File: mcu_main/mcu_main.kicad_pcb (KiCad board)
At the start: 2 copper layers, 108 x 61.7 mm, 48 parts, among them J1 Micro_SD_Card_Det_Hirose_DM3AT, J10 Conn_01x02_Pin, J2 Conn_01x10_Pin, J3 Conn_01x06_Pin, J4 4P4C_Shielded, J5 4P4C_Shielded, J6 Screw_Terminal_01x03_ebrake, J7 Screw_Terminal_01x03_throttle, J8 Screw_Terminal_01x06, J9 Conn_01x14_Socket, U1 ESP32-S3-WROOM-1, U2 USB_C_connector, U3 SGM2212-3.3, U4 VL53L1CXV0FY1, sw1 SW_Push_Dual, sw2 SW_Push_Dual

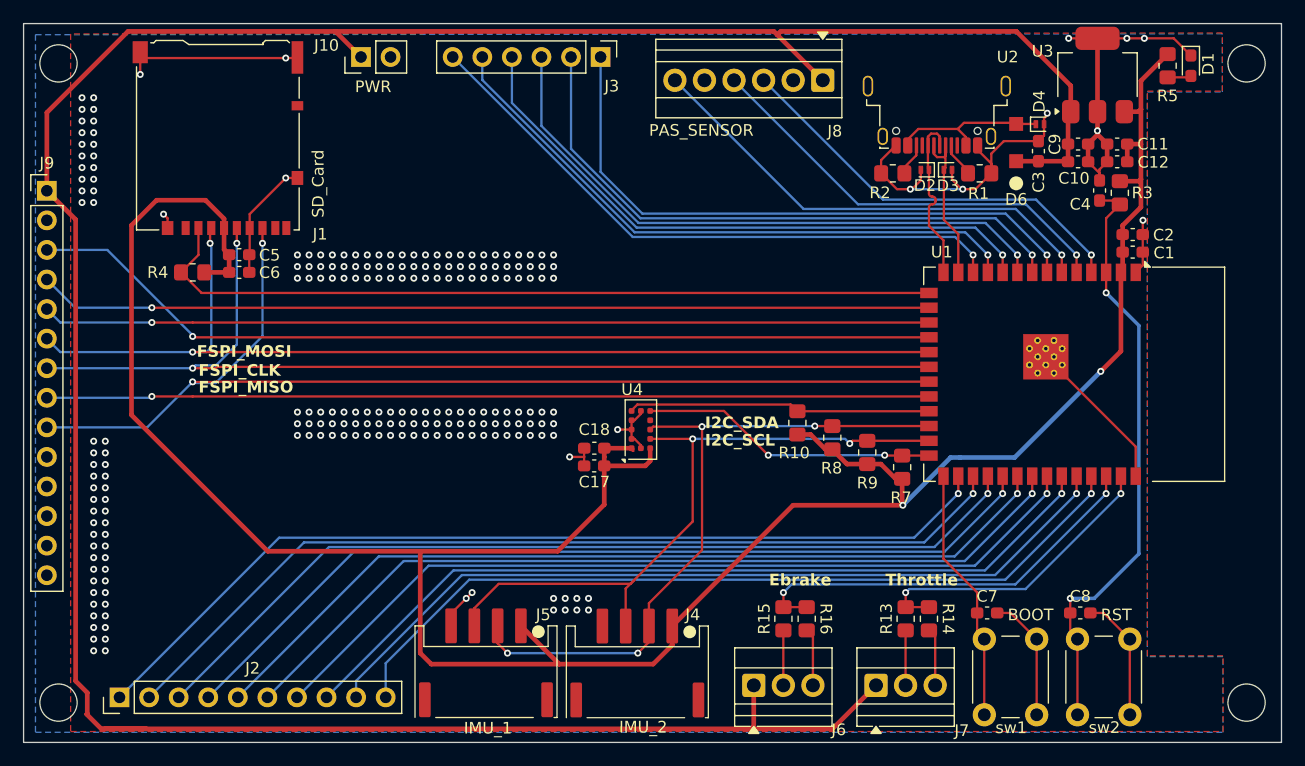
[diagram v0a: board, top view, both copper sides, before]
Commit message: stitching vias
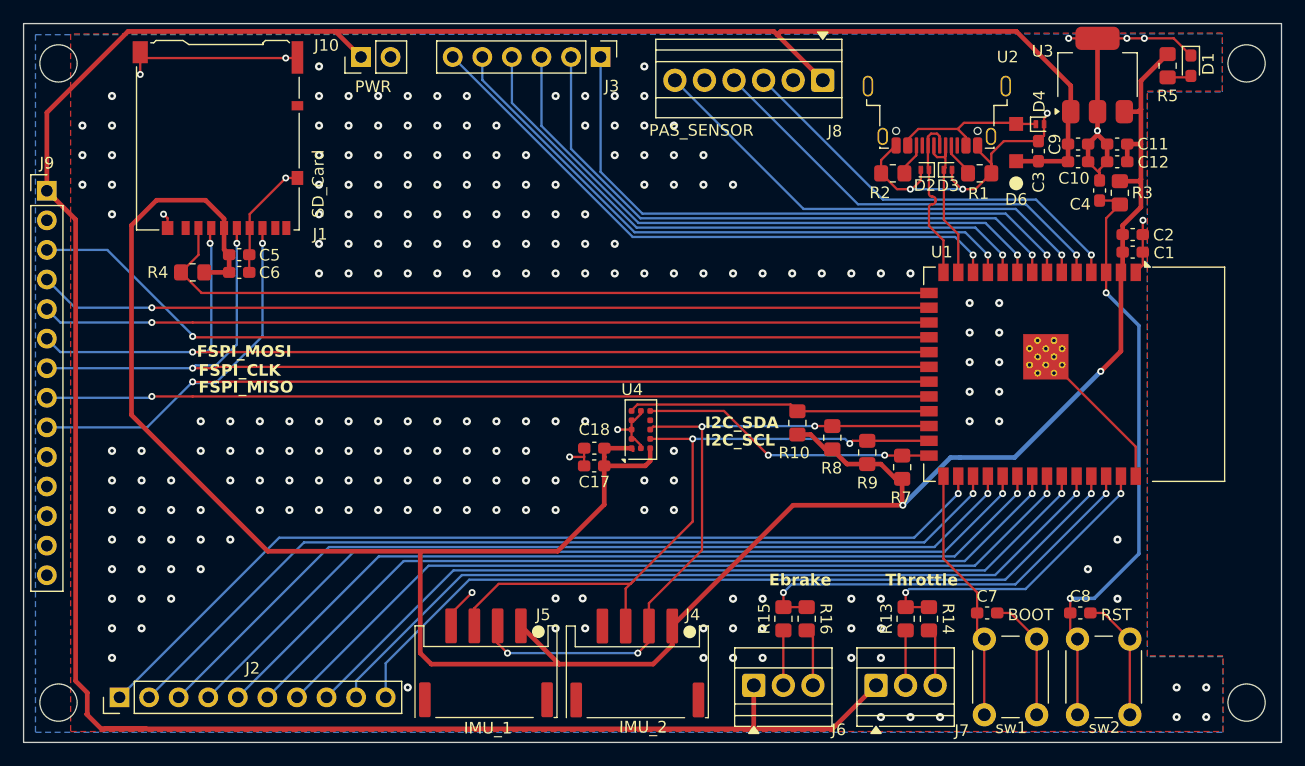
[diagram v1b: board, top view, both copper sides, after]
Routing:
- net GND: vias 220 -> 230

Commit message: test points and silkscreen annotations
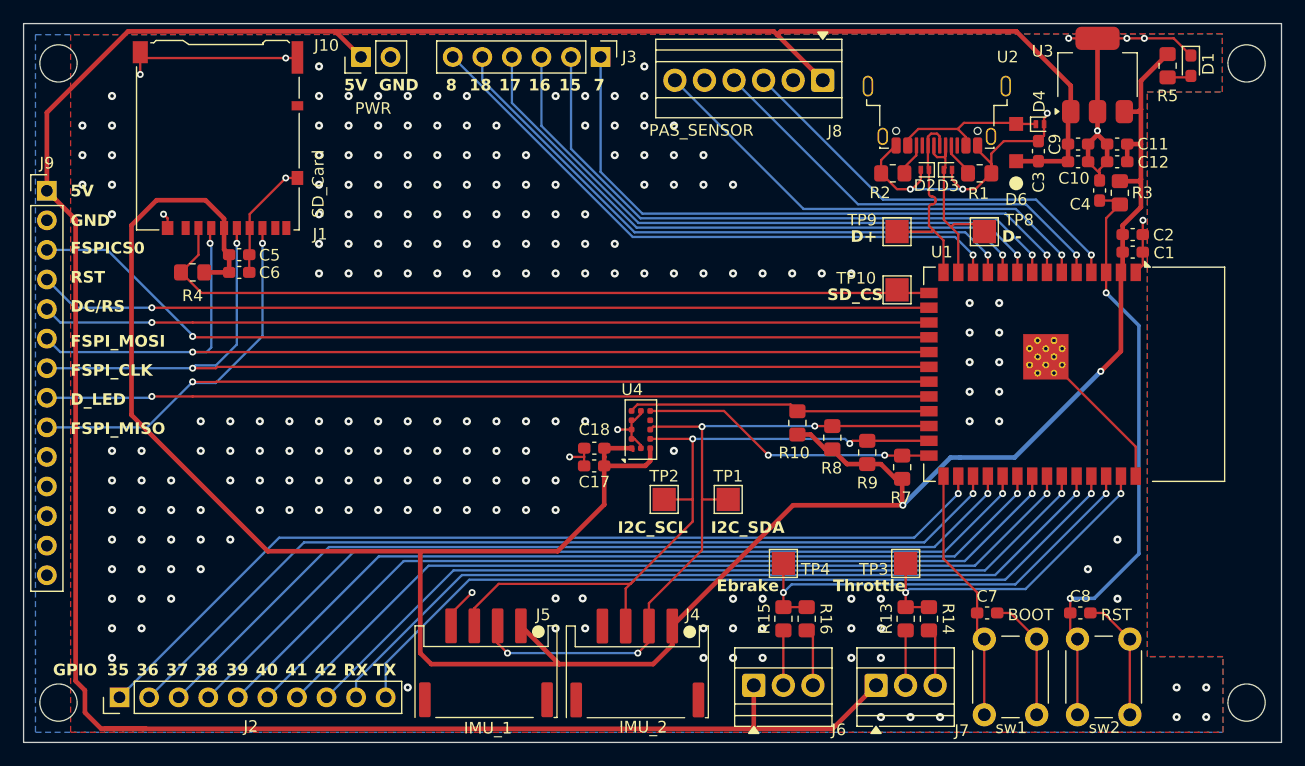
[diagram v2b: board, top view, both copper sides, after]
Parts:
- added TP1: TestPoint, TestPoint:TestPoint_Pad_2.0x2.0mm, F.Cu at (160.5, 110.9)
- added TP10: TestPoint, TestPoint:TestPoint_Pad_2.0x2.0mm, F.Cu at (175.0, 92.9)
- added TP2: TestPoint, TestPoint:TestPoint_Pad_2.0x2.0mm, F.Cu at (155.0, 110.9)
- added TP3: TestPoint, TestPoint:TestPoint_Pad_2.0x2.0mm, F.Cu at (175.8, 116.4)
- added TP4: TestPoint, TestPoint:TestPoint_Pad_2.0x2.0mm, F.Cu at (165.3, 116.4)
- added TP8: TestPoint, TestPoint:TestPoint_Pad_2.0x2.0mm, F.Cu at (182.5, 87.9)
- added TP9: TestPoint, TestPoint:TestPoint_Pad_2.0x2.0mm, F.Cu at (175.0, 87.9)
- C3: value 10uF 25V -> 10uF
- C4: value 1uF 16V -> 1uF
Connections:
- net /ESP USB section/D+ renamed Data+
- net /ESP USB section/D- renamed Data-
- net /PAS connector/speed_sig_1 renamed speed_1
- net /PAS connector/speed_sig_2 renamed speed_2
- net /PAS connector/torque_sig renamed Torque
- net /Throttle and ebrake connectors/ebrake_sig renamed Ebrake_sig
- net /Throttle and ebrake connectors/throttle_sig renamed Throttle_sig
- net /Time of flight sensor/TOF_GPIO1 renamed TOF_GPIO1
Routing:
- net Data-: track 14.8 -> 18.1 mm
- net Data+: track 14.8 -> 18.0 mm
- net Throttle_sig: track 26.8 -> 29.3 mm
- net Ebrake_sig: track 36.0 -> 38.5 mm
- net I2C_SDA: track 59.7 -> 62.0 mm
- net I2C_SCL: track 58.9 -> 60.9 mm
- net GND: vias 230 -> 224
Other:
- board text added: "15"
- board text added: "16"
- board text added: "17"
- board text added: "18"
- board text added: "35"
- board text added: "36"
- board text added: "37"
- board text added: "38"
- board text added: "39"
- board text added: "40"
- board text added: "41"
- board text added: "42"
- board text added: "5V"
- board text added: "7"
- board text added: "8"
- board text added: "D+"
- board text added: "D-"
- board text added: "DC/RS"
- board text added: "D_LED"
- board text added: "FSPICS0"
- board text added: "GND"
- board text added: "GPIO"
- board text added: "RX"
- board text added: "SD_CS"
- board text added: "TX"
